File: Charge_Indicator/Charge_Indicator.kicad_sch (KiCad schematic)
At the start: 68 parts, among them J1 PZ254-2-02-S, J2 1711725, J3 1711725, J4 PZ254-2-02-S, M1 M3, M2 M3, M3 M3, M4 M3, SW1 SSSS811101, U1 BQ34Z100-R2, U2 SGM61410XN6G_TR, U3 INA226, U4 SN74HC164PWR, U5 TLV74033PDQNR

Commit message: Finished routing, might need some changes
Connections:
- net AGND: now also C1.2 (1), C12.2 (1), C13.2 (1), C3.2 (1), C5.2 (1), C6.2 (1), C7.2 (1), C8.1, D1.1 (A), D7.1 (A), D8.1 (A), D9.1 (A), J1.3, J2.1, J4.3, M1.1, M2.1, M3.1, M4.1, R19.2, R20.1, R3.2, U2.2 (GND), U3.1 (A1), U3.2 (A0), U3.7 (GND), U4.7 (GND), U5.2 (GND), U5.5 (GND)
- removed net GND: C1.2 (1), C12.2 (1), C13.2 (1), C3.2 (1), C5.2 (1), C6.2 (1), C7.2 (1), C8.1, D1.1 (A), D7.1 (A), D8.1 (A), D9.1 (A), J1.3, J2.1, J3.2, J4.3, R19.1, R19.2, R20.1, R21.1, R3.2, U2.2 (GND), U3.1 (A1), U3.2 (A0), U3.7 (GND), U4.7 (GND), U5.2 (GND), U5.5 (GND)
- new net BAT-: J3.2, R19.1, R21.1
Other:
- note added: "Current Sense (High Side)"
- note added: "Current Sense (Low Side)"
- note added: "the input voltage generated across the current sense resistor should not exceed +/-125 mV"
- moved on the sheet: FID1, FID2, FID3

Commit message: SW1 Wiring - fix
Summary of Changes:
- Pin 2 of the switch is now connected to R17.
- M on the switch is now on Ground.
- Re-routed on PCB side, now ground polygons span entire PCB to encompass switch grounds.
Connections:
- net AGND: now also SW1.M
- net at R17.1: now also SW1.2; no longer SW1.M
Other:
- moved on the sheet: SW1

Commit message: Global Label vs Power Symbol vs NetLabel fix
Summary of Changes:
- Global labels are now Net Labels.
- Power rails now have their own power symbol.
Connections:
- net 3.3V renamed +3v3
- net 5V renamed +5v

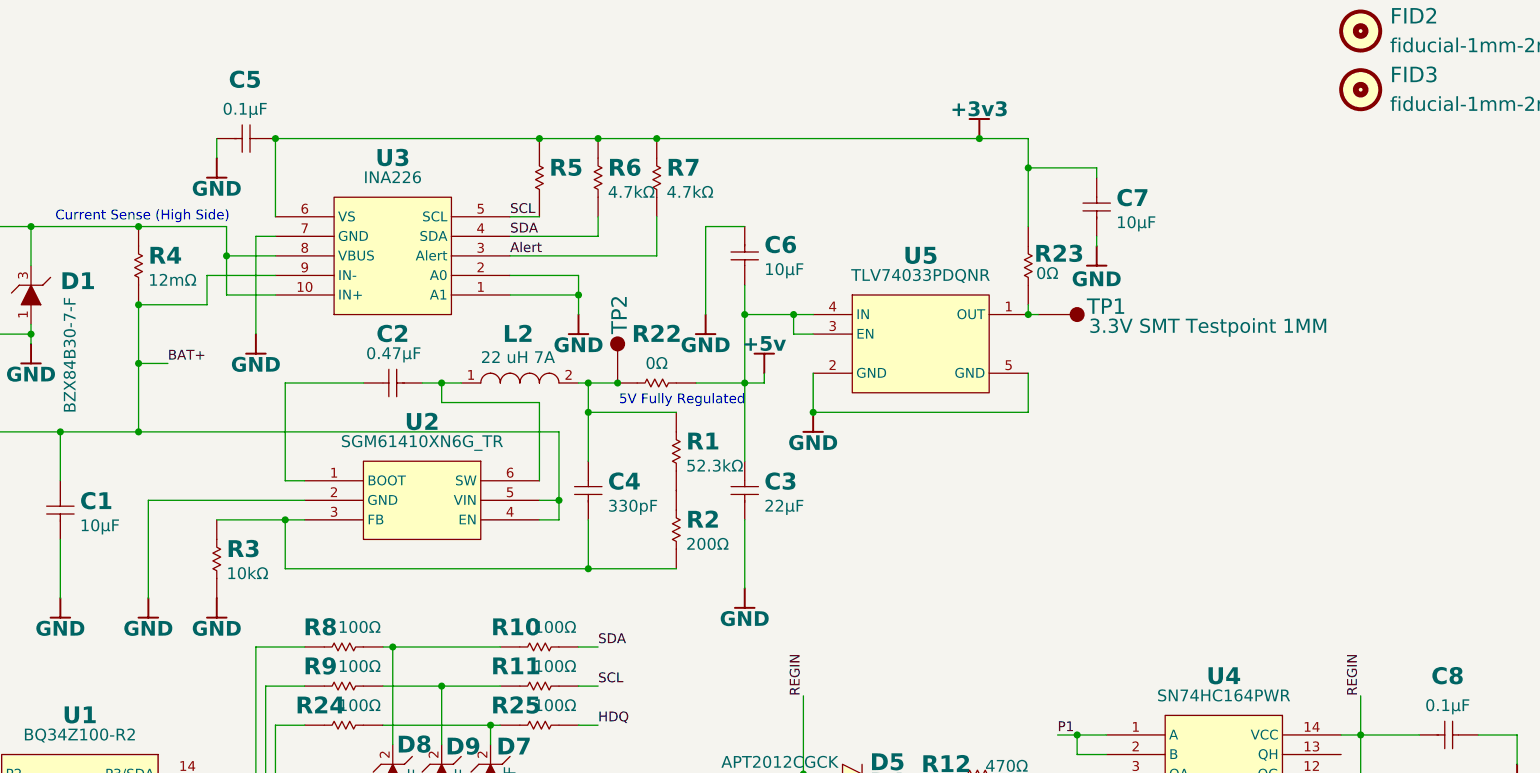
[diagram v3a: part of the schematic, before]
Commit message: Move output caps fix
Summary of Changes:
- 5v0 and 3v3 lines now have their decoupling capacitors next to the test points before the 0 Ohm resistors.
- Reroute to carry the change to the PCB.
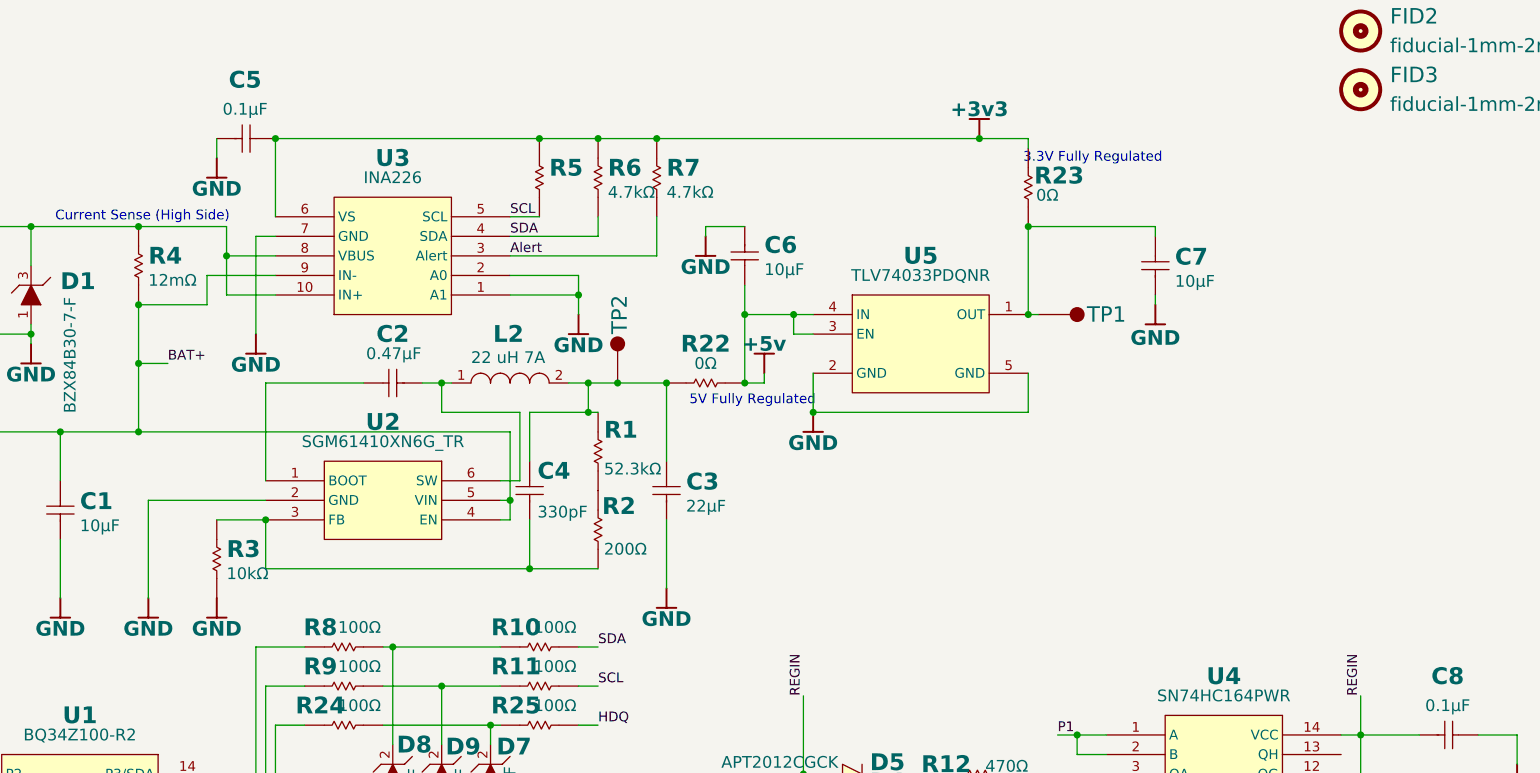
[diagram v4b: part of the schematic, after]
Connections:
- net +3v3: no longer C7.1
- net +5v: no longer C3.1
- net at R23.1, TP1.1, U5.1 (OUT): now also C7.1
- net at C4.1, L2.2, R1.1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: now also C3.1
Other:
- note added: "3.3V Fully Regulated"
- moved on the sheet: C3, C4, C7, L2, R1, R2, R22, R23, U2

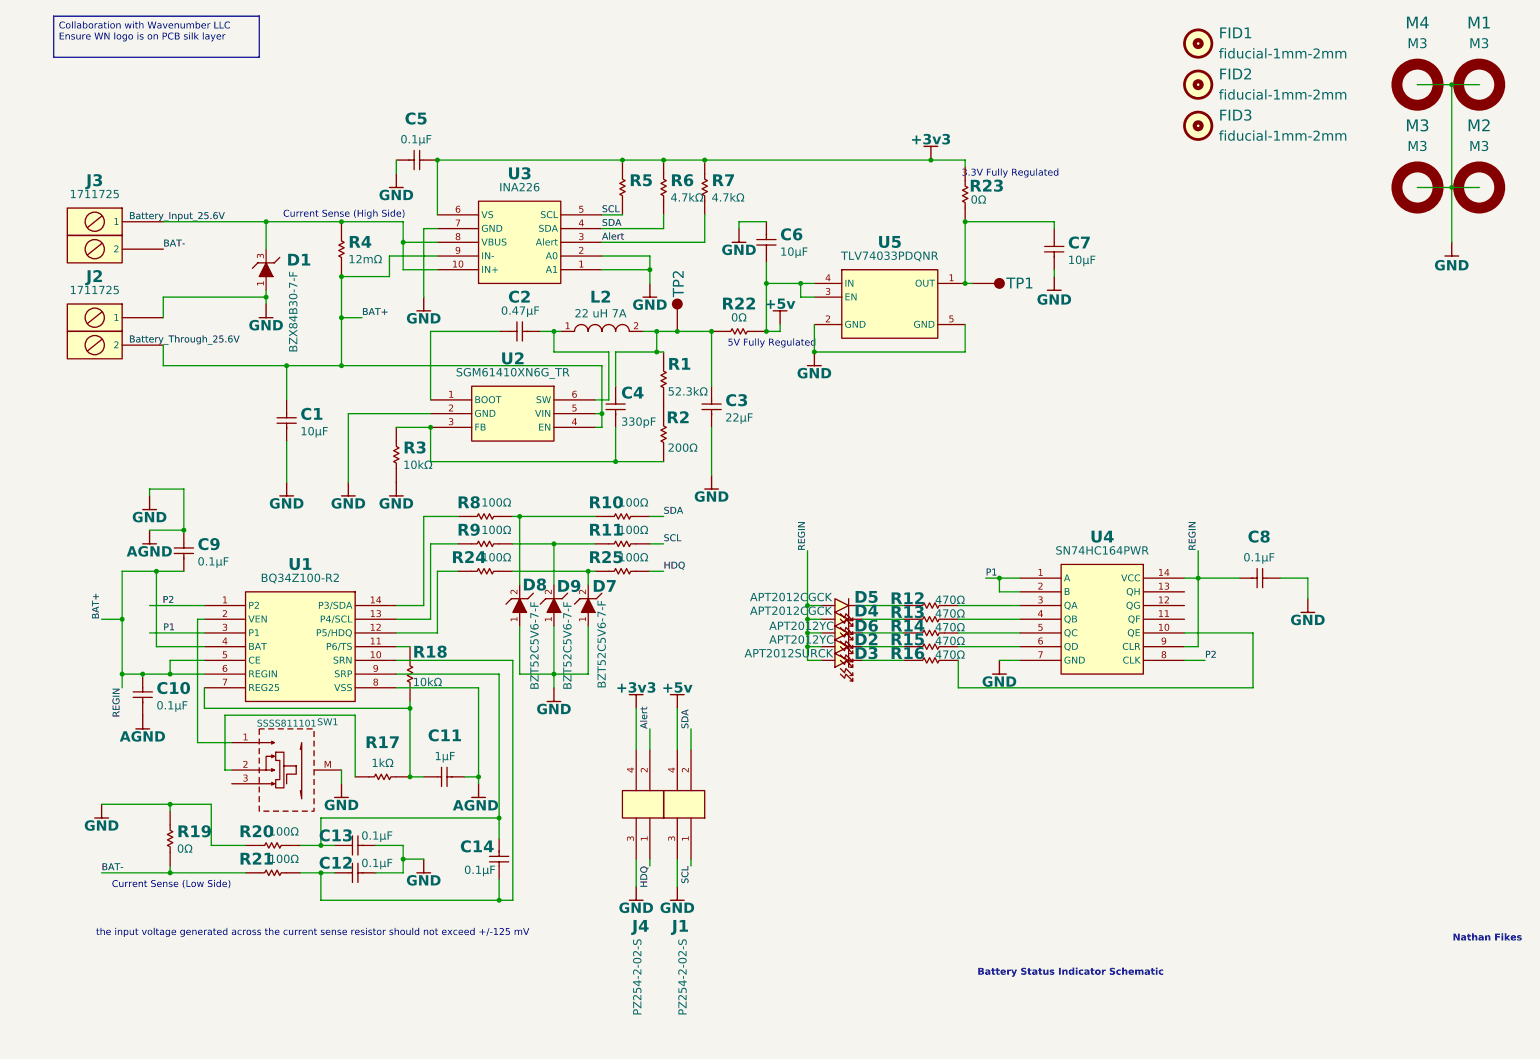
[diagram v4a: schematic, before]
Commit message: Sch Style / Intent fix
Summary of Changes:
- Major overhaul to how the Schematic side is presented. Now the Sch side is in blocks.
- Some symbols were updated to create more space and ease of viewing.
- New lower side current sense resistor at 0.005 Ohms at 2.5 W.
- New PCB silkscreen Layer items.
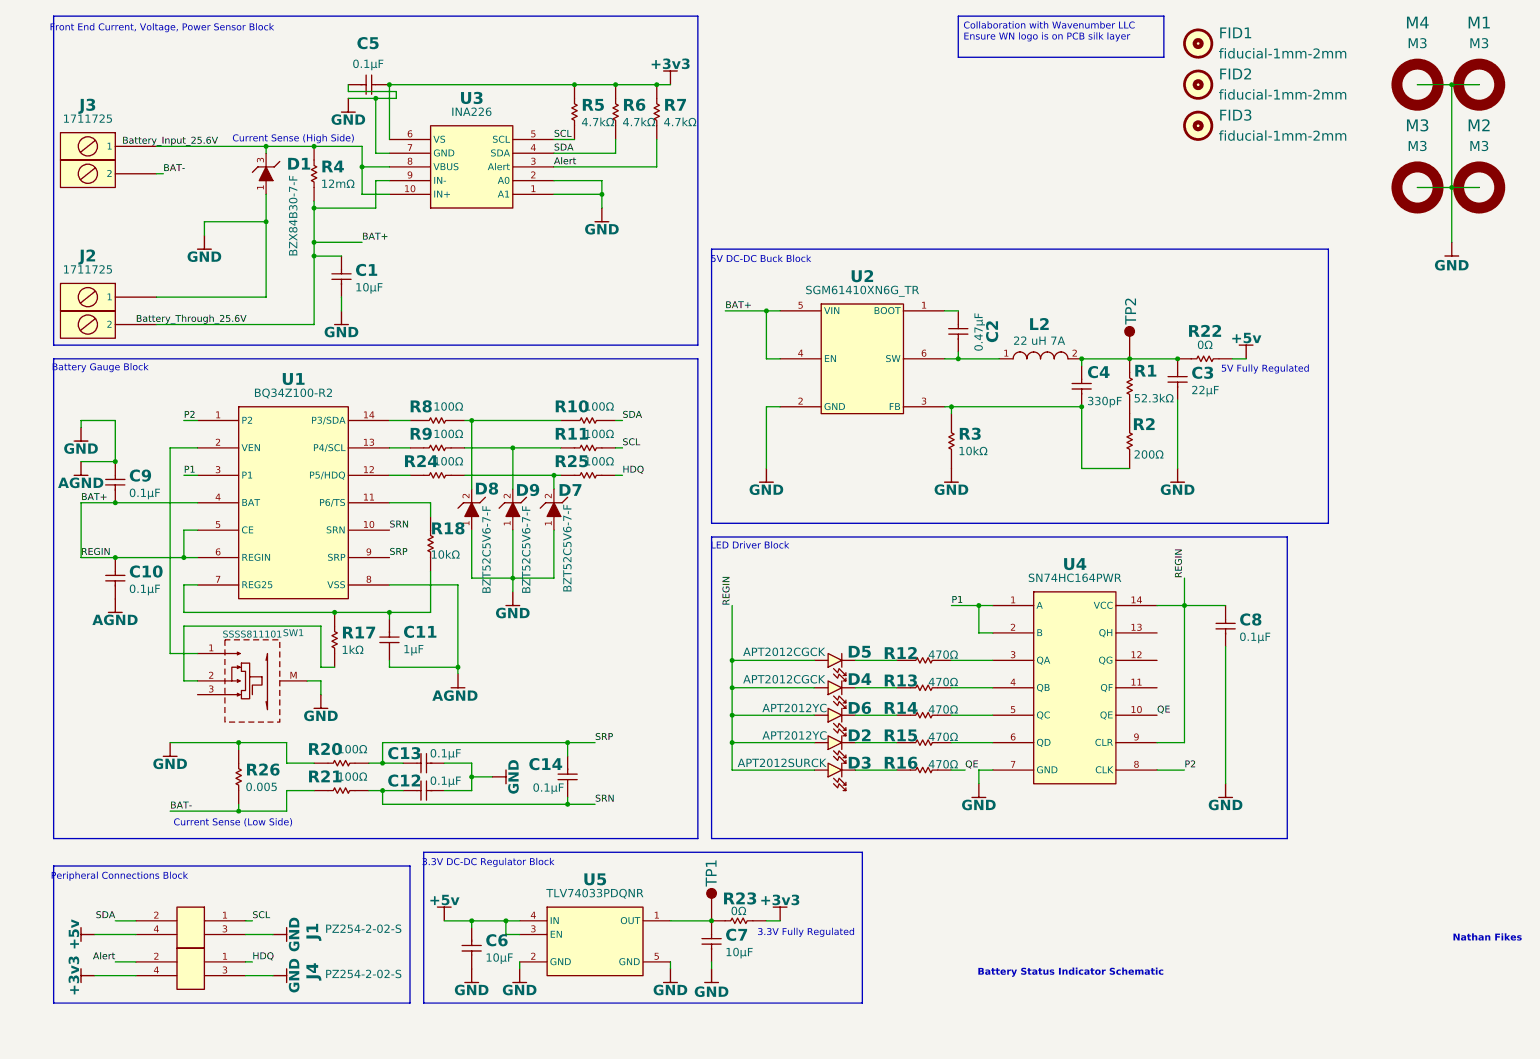
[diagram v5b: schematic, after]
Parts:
- removed R19: 0Ω, wavenumber:R0201_0.26MM_HD, symbol wn__wavenumber:R_2P
- added R26: 0.005, wavenumber:R2512_MD, symbol wn__wavenumber:CSR2512B0R005F
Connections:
- net +3v3: now also R23.1; no longer R23.2
- net +5v: now also C6.2 (1); no longer C6.1
- net AGND: now also C11.1, C6.1, C8.2 (1), R26.2; no longer C11.2 (1), C6.2 (1), C8.1
- net BAT+: now also C8.1; no longer C8.2 (1)
- net BAT-: now also R26.1
- net at R17.2, R18.1, U1.7 (REG25): now also C11.2 (1); no longer C11.1
- net SRN: now reaches C12.1, C14.1, R21.2, U1.10 (SRN)
- net SRP: now reaches C13.1, C14.2 (1), R20.2, U1.9 (SRP)
- net at C7.1, TP1.1, U5.1 (OUT): now also R23.2; no longer R23.1
- net QE: now reaches R16.2, U4.10 (QE)
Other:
- note added: "3.3V DC-DC Regulator Block"
- note added: "5V DC-DC Buck Block"
- note added: "Battery Gauge Block"
- note added: "Front End Current, Voltage, Power Sensor Block"
- note added: "LED Driver Block"
- note added: "Peripheral Connections Block"
- note removed: "the input voltage generated across the current sense resistor should not exceed +/-125 mV"
- moved on the sheet: C1, C10, C11, C12, C13, C14, C2, C3, C4, C5, C6, C7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
